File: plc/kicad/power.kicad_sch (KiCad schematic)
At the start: 82 parts, among them Q5 BSS138LT1G, Q6 CSD19537Q3, SW3 TSD003B08026A03, U14 LMR16006XDDCR, U15 TPS54560DDAR, U16 TPS26630RGER, U17 TLV76733DRVR

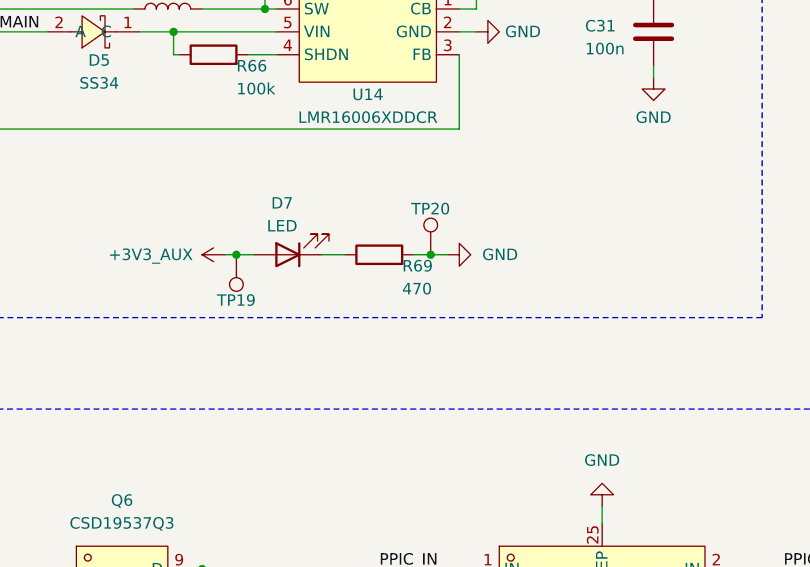
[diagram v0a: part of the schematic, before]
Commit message: Added setup leds & shared SPI bus
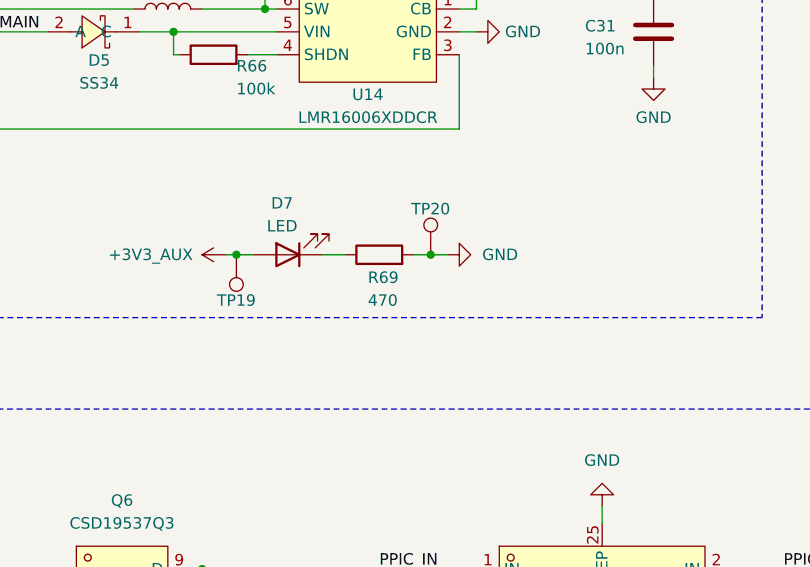
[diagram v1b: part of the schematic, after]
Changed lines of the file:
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@@
 		(dnp no)
 		(property "Reference" "R69"
-			(at 107.95 147.955 90)
+			(at 104.14 149.225 90)
 			(show_name no)
 			(do_not_autoplace no)
@@
 		)
 		(property "Value" "470"
-			(at 107.95 150.495 90)
+			(at 104.14 151.765 90)
 			(show_name no)
 			(do_not_autoplace no)

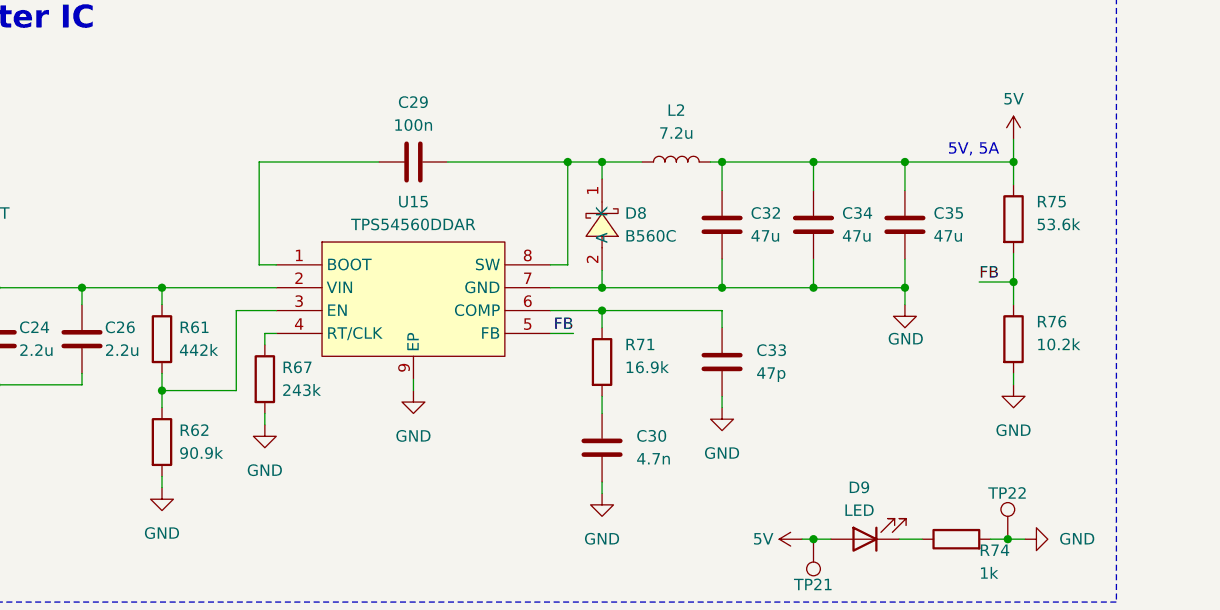
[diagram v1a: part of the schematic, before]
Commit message: TPS54560 changed to TPS54560B
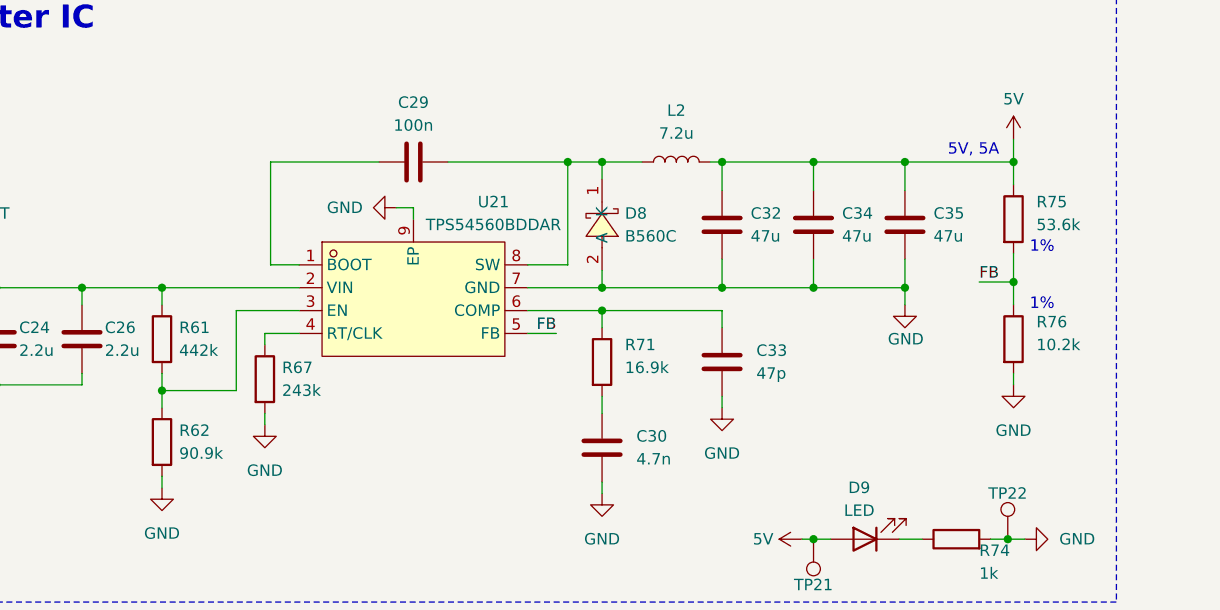
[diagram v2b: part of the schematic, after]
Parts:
- removed U15: TPS54560DDAR, LibrePLC32:SOIC-8_L5.0-W4.0-P1.27-LS6.0-BL-EP2.0, symbol LibrePLC32:TPS54560DDAR
- added U21: TPS54560BDDAR, LibrePLC32:POWERPAD-SO-8_L4.9-W3.9-P1.27-LS6.0-BL-EP, symbol LibrePLC32:TPS54560BDDAR
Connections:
- net FB: now also U21.5 (FB)
- net GND: now also U21.7 (GND), U21.9 (EP)
- net at C20.1, C23.1, C24.1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: now also U21.2 (VIN)
- net at C29.1: now also U21.1 (BOOT)
- net at R61.2, R62.1: now also U21.3 (EN)
- net at R67.1: now also U21.4 (RT/CLK)
- net at C33.2, R71.1: now also U21.6 (COMP)
- net at C29.2, D8.1 (K), L2.1: now also U21.8 (SW)
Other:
- note added: "1%"

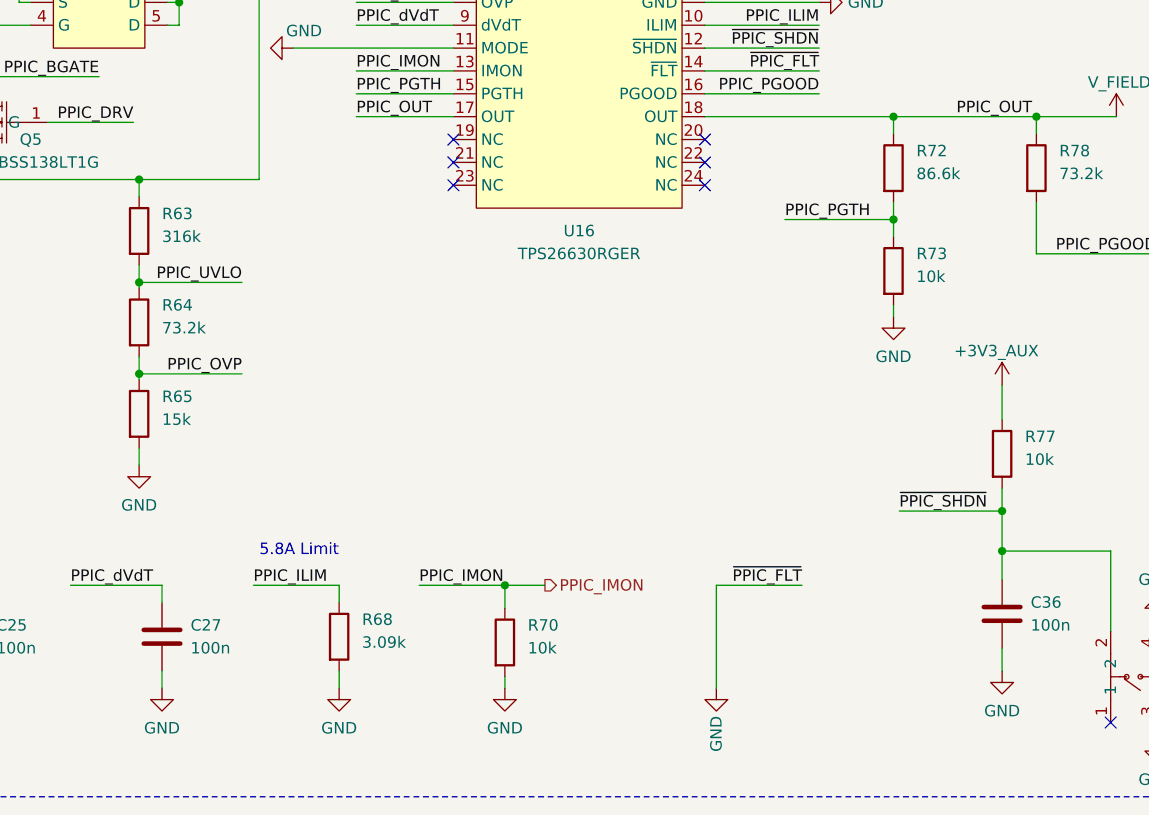
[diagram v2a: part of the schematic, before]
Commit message: Modified TPS26630 resistor values
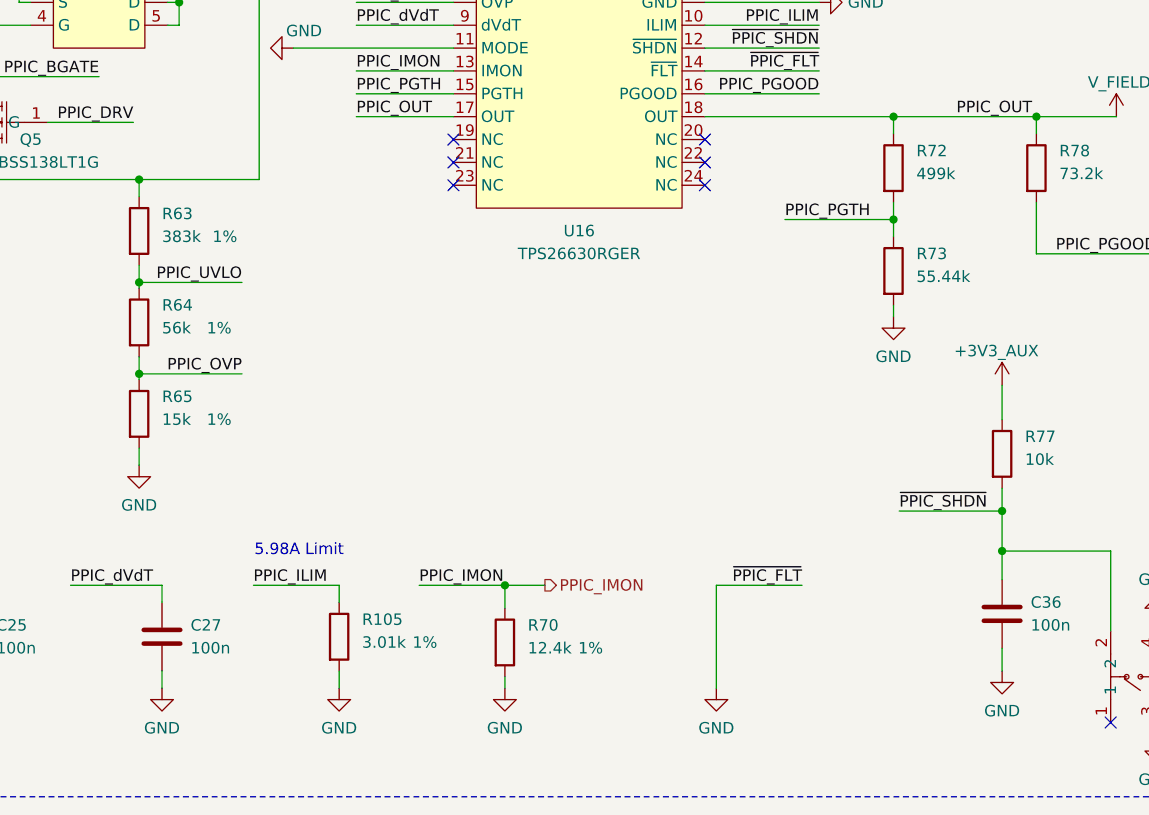
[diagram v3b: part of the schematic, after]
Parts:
- removed R68: 3.09k, Resistor_SMD:R_0603_1608Metric, symbol Device:R
- added R105: 3.01k, Resistor_SMD:R_0603_1608Metric, symbol Device:R
- R63: value 316k -> 383k; Tolerance (none) -> 1%
- R64: value 73.2k -> 56k; Tolerance (none) -> 1%
- R65: Tolerance (none) -> 1%
- R70: value 10k -> 12.4k; Tolerance (none) -> 1%
- R72: value 86.6k -> 499k
- R73: value 10k -> 55.44k
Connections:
- net GND: now also R105.2
- net PPIC_ILIM: now also R105.1
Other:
- note added: "5.98A Limit"
- note removed: "5.8A Limit"

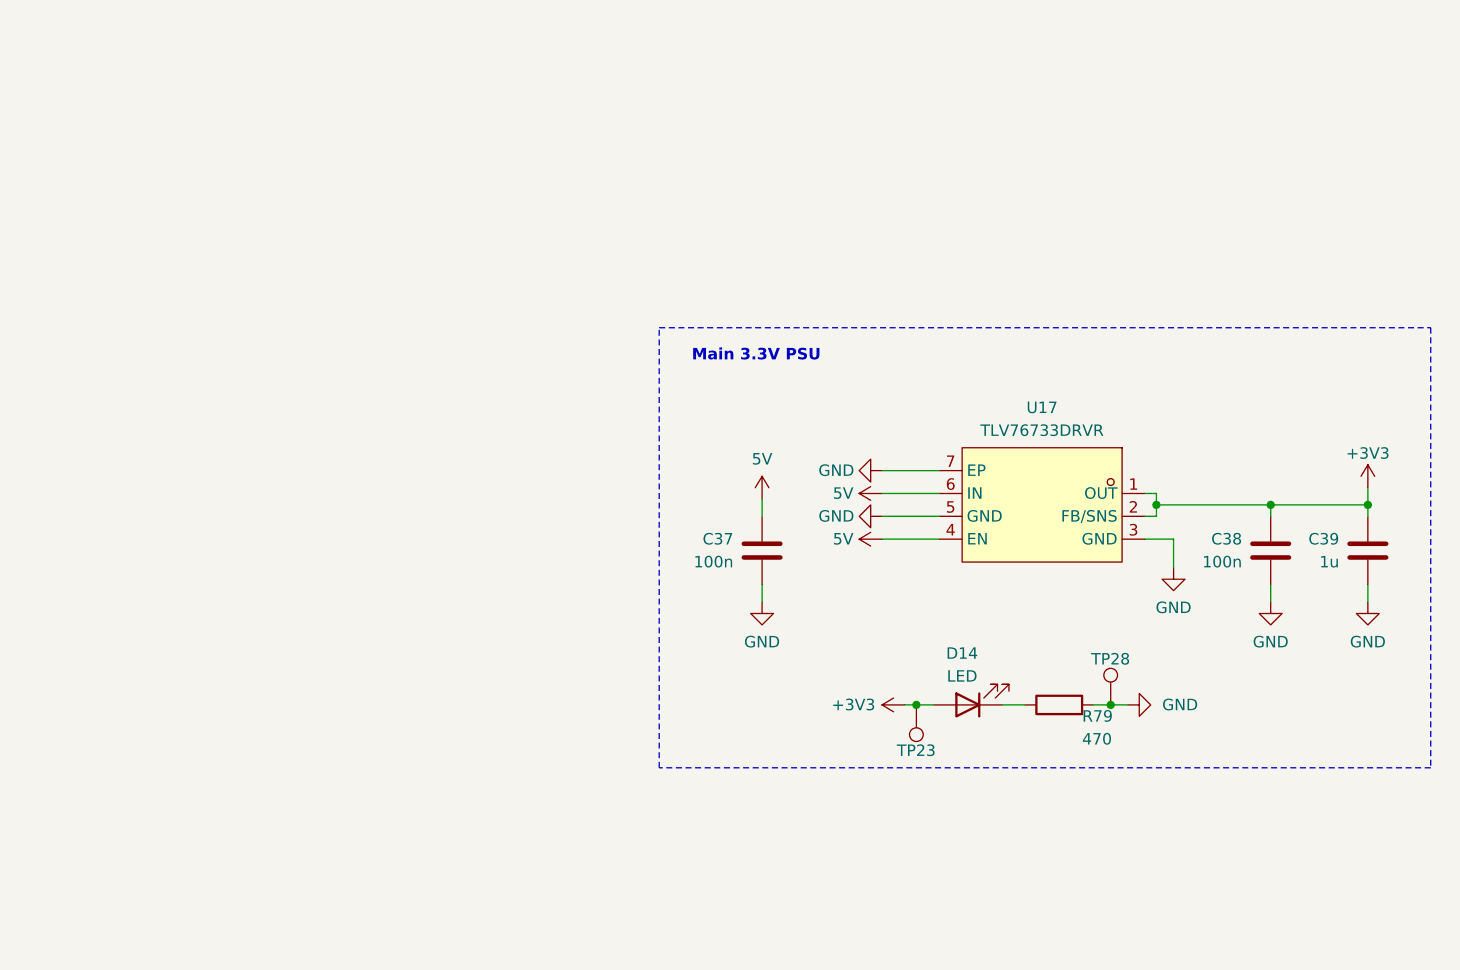
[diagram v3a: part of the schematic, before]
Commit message: Changed TLV76733 to TPS7A52-Q1
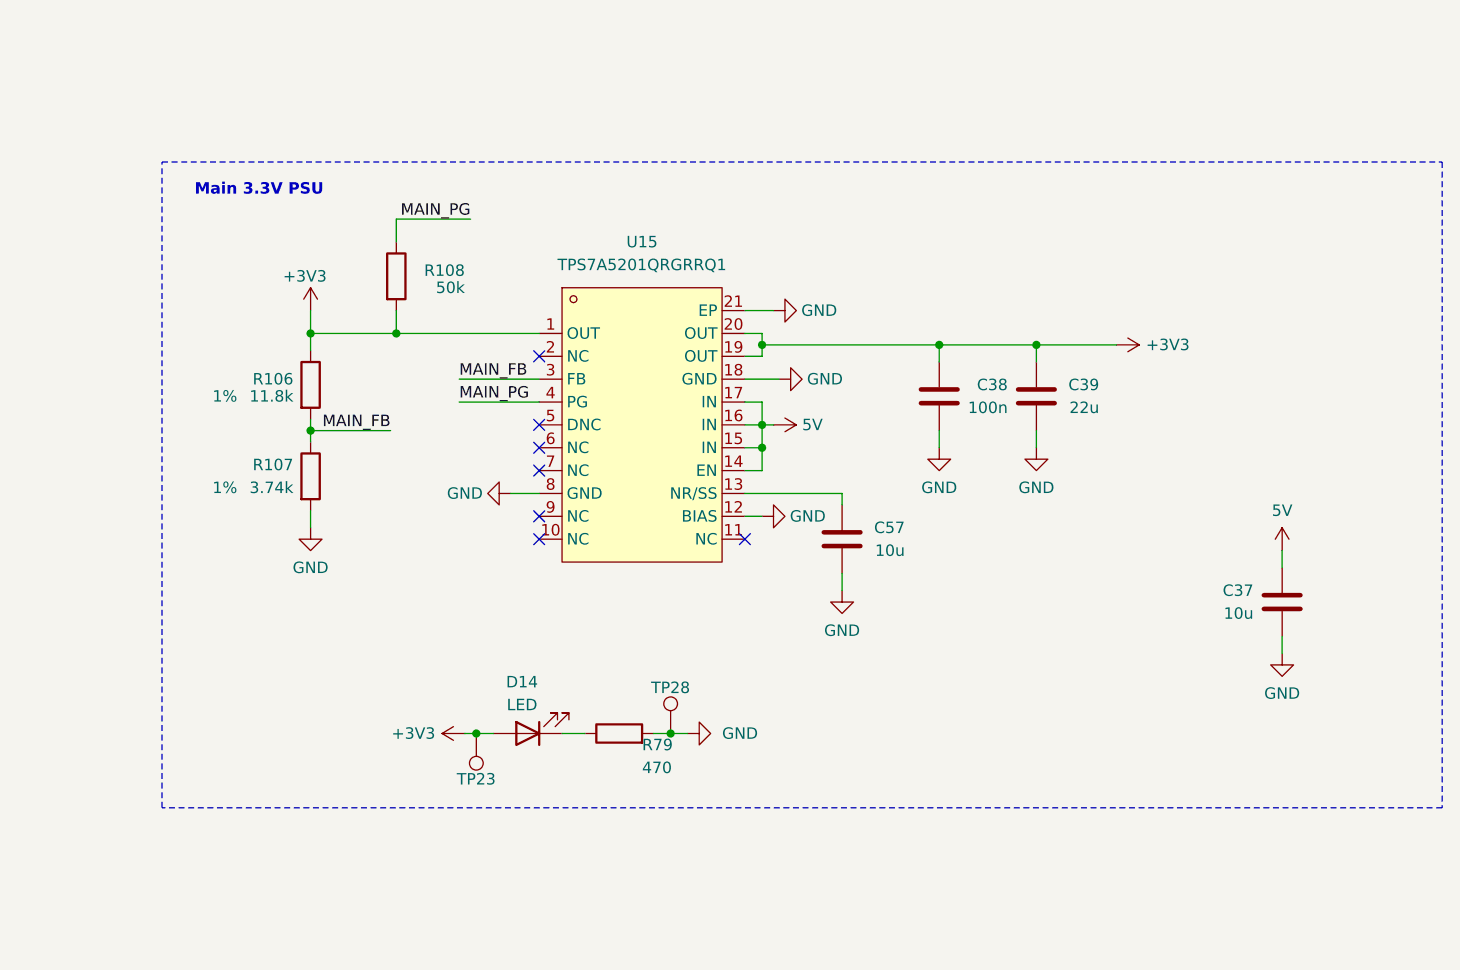
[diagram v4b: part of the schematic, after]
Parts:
- removed U17: TLV76733DRVR, LibrePLC32:WSON-6_L2.0-W2.0-P0.65-TL-EP, symbol LibrePLC32:TLV76733DRVR
- added C57: 10u, Capacitor_SMD:C_0603_1608Metric, symbol Device:C
- added R106: 11.8k, Resistor_SMD:R_0603_1608Metric, symbol Device:R
- added R107: 3.74k, Resistor_SMD:R_0603_1608Metric, symbol Device:R
- added R108: 50k, Resistor_SMD:R_0603_1608Metric, symbol Device:R
- added U15: TPS7A5201QRGRRQ1, LibrePLC32:VQFN-20_L3.5-W3.5-P0.50-TL-EP, symbol LibrePLC32:TPS7A5201QRGRRQ1
- C37: value 100n -> 10u
- C39: value 1u -> 22u
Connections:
- net +3V3: now also R106.1, R108.2, U15.1 (OUT), U15.19 (OUT), U15.20 (OUT)
- net 5V: now also U15.14 (EN), U15.15 (IN), U15.16 (IN), U15.17 (IN)
- net GND: now also C57.1, R107.2, U15.12 (BIAS), U15.18 (GND), U15.21 (EP), U15.8 (GND)
- new net: C57.2, U15.13 (NR/SS)
- new net MAIN_FB: R106.2, R107.1, U15.3 (FB)
- new net MAIN_PG: R108.1, U15.4 (PG)
- no-connect marks 7 -> 14
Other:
- moved on the sheet: D14, R79, TP23, TP28

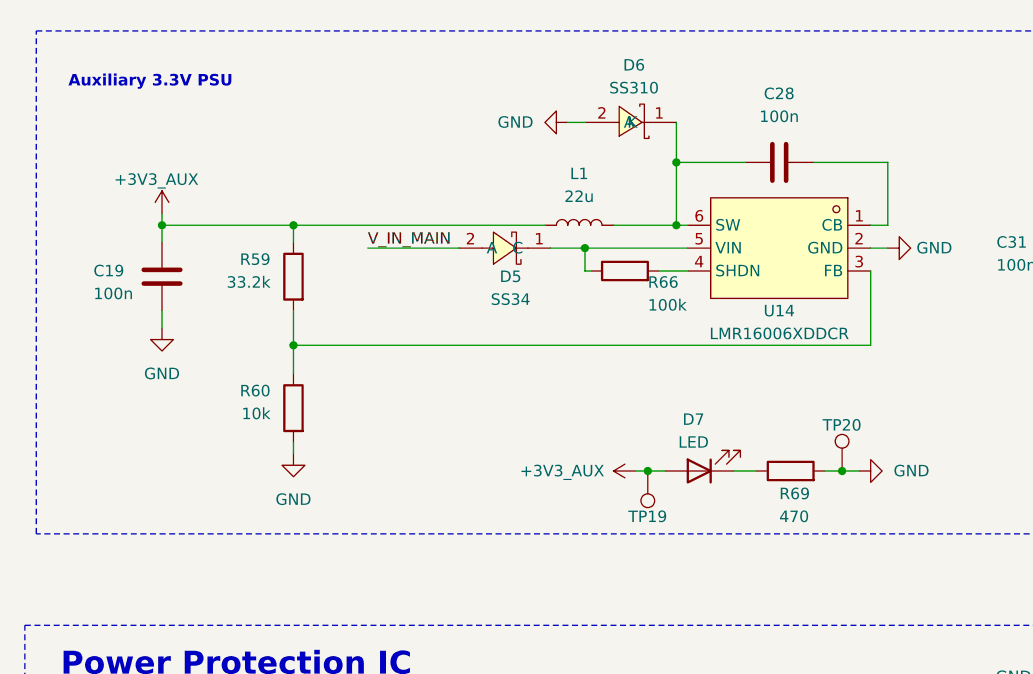
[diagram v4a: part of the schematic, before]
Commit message: Updated LMR16006X circuit
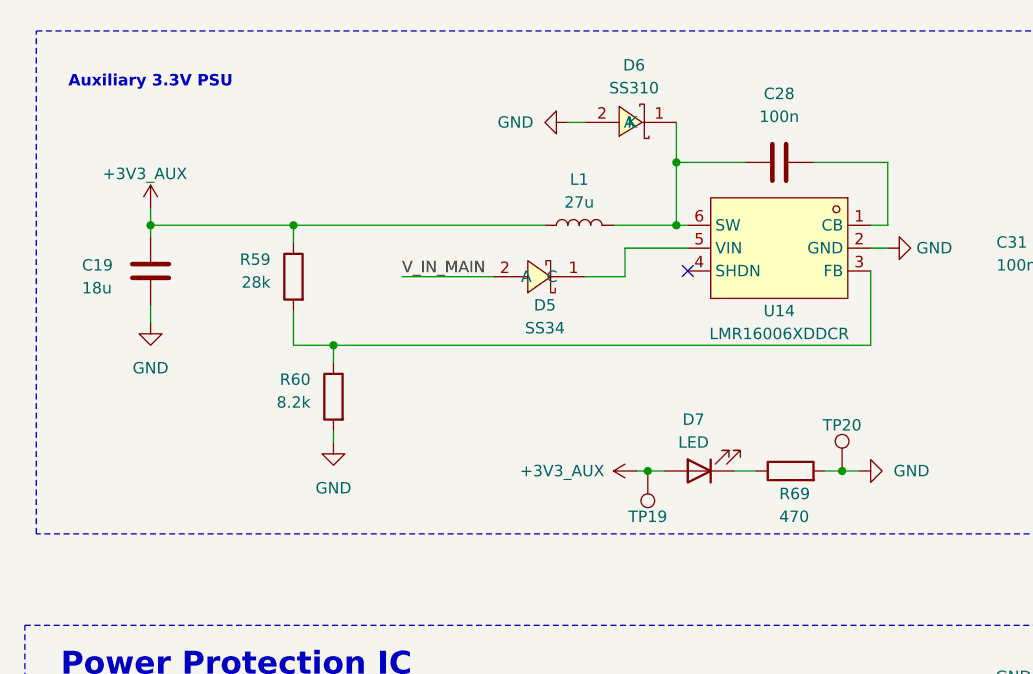
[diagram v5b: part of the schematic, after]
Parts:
- removed R66: 100k, Resistor_SMD:R_0603_1608Metric, symbol Device:R
- C19: value 100n -> 18u
- L1: value 22u -> 27u
- R59: value 33.2k -> 28k
- R60: value 10k -> 8.2k
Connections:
- no-connect marks 14 -> 15
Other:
- moved on the sheet: C19, D5, R60
